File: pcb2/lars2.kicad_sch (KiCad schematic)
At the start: 35 parts, among them SW1 Encoder, SW10 SW_Push, SW2 SW_Push, SW3 SW_Push, SW4 SW_Push, SW5 SW_Push, SW6 SW_Push, SW7 SW_Push, SW8 SW_Push, SW9 SW_Push, U1 Pico, U2 Charger, U3 MOSFET, U4 MOSFET, U5 MOSFET, U6 STEP_UP, U7 STEP_UP, U8 STEP_UP

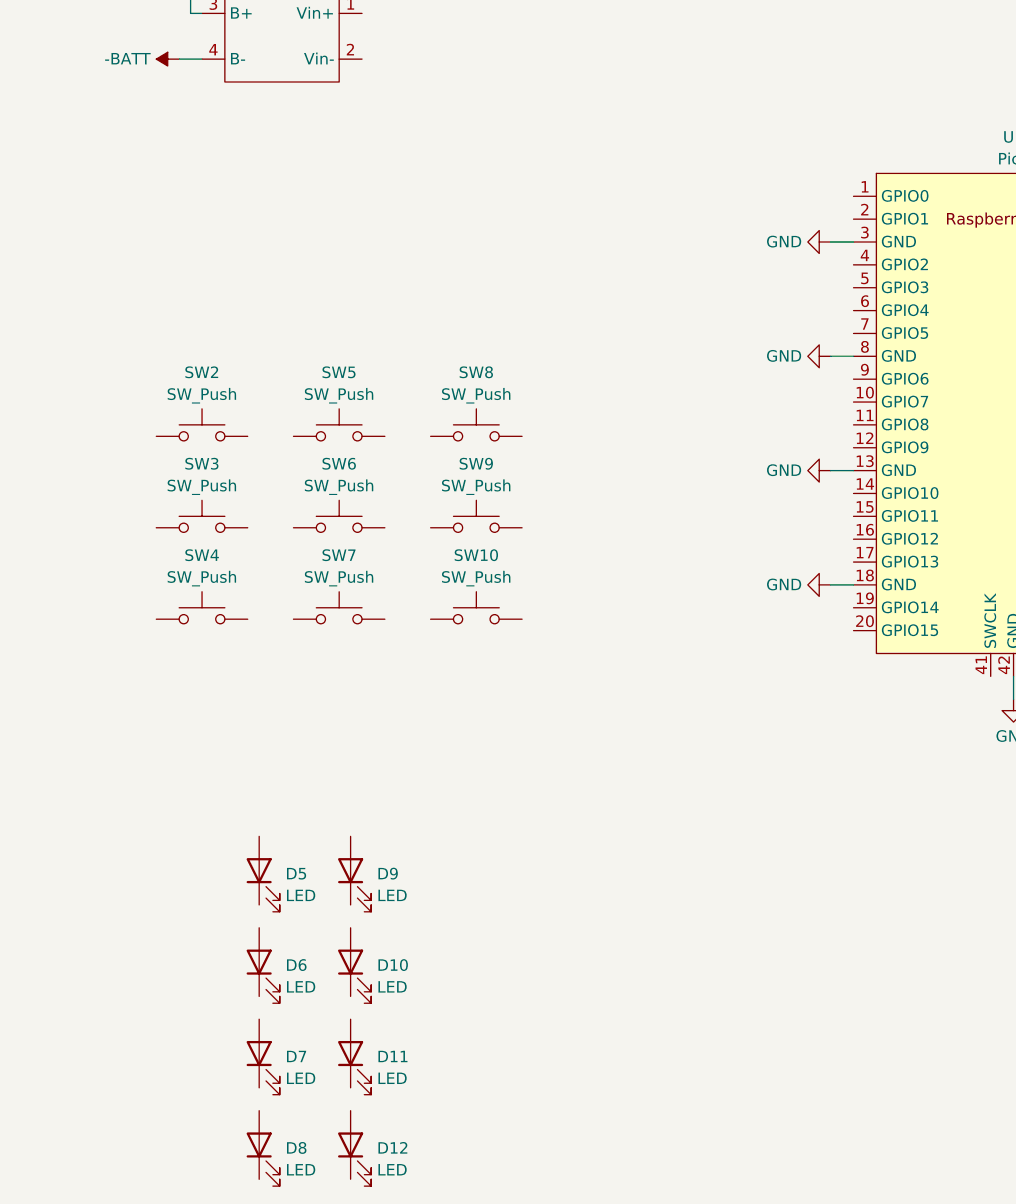
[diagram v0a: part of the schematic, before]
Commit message: finish pcb2, now with buttons and leds
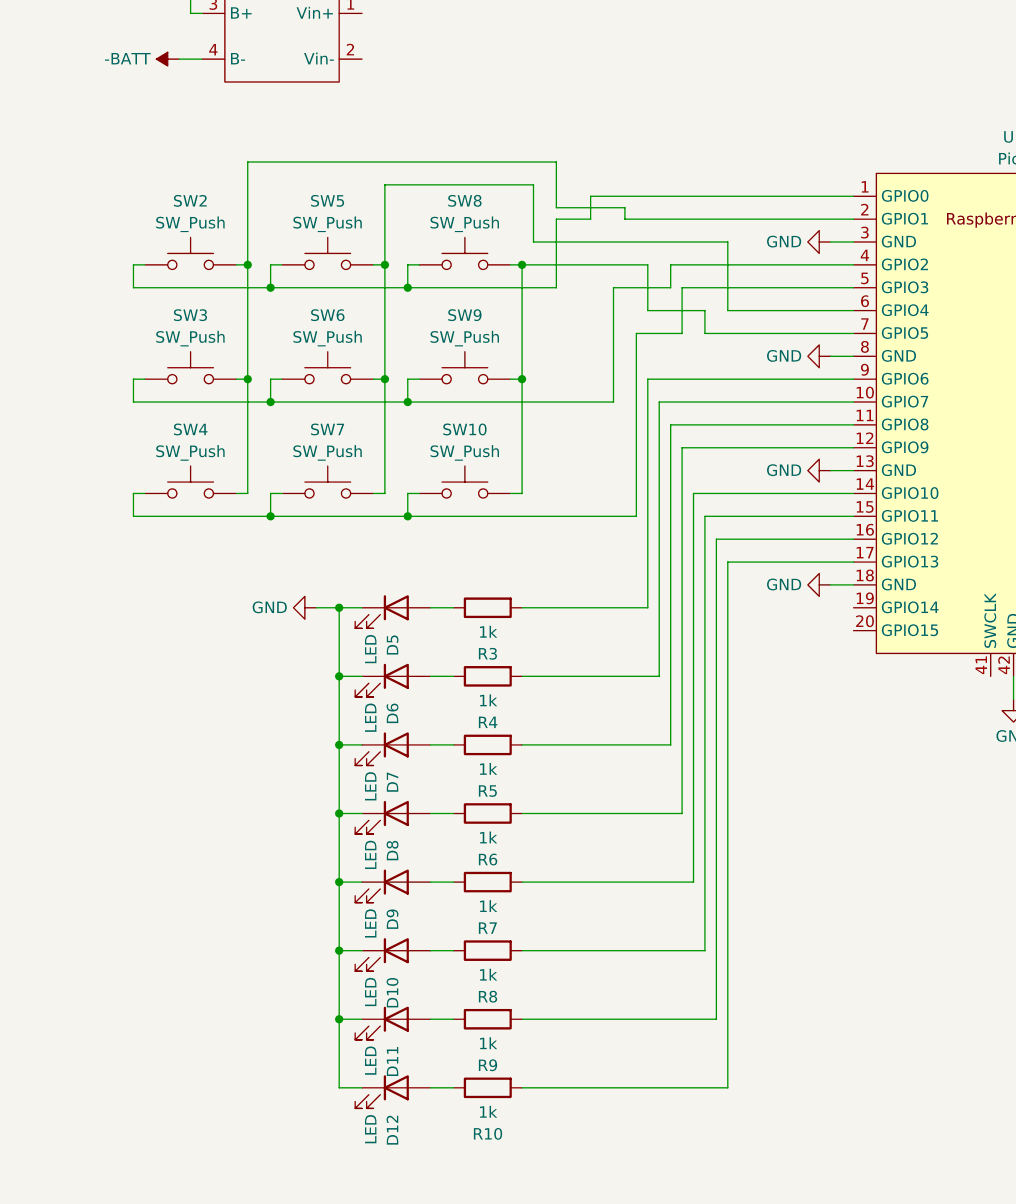
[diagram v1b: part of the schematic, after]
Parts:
- added R10, R3, R4, R5, R6, R7, R8, R9: 1k, Resistor_THT:R_Axial_DIN0204_L3.6mm_D1.6mm_P2.54mm_Vertical, symbol Device:R
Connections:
- net -BATT: now also D10.1 (K), D11.1 (K), D12.1 (K), D5.1 (K), D6.1 (K), D7.1 (K), D8.1 (K), D9.1 (K)
- net at D11.2 (A): now also R9.1
- net at D6.2 (A): now also R4.1
- net at SW3.1: now also SW6.1, SW9.1, U1.4 (GPIO2)
- net at SW3.2: now also SW2.2, SW4.2, U1.2 (GPIO1)
- net at SW7.1: now also SW10.1, SW4.1, U1.5 (GPIO3)
- net at SW7.2: now also SW5.2, SW6.2, U1.6 (GPIO4)
- net at D9.2 (A): now also R7.1
- net at SW2.1: now also SW5.1, SW8.1, U1.1 (GPIO0)
- net at D10.2 (A): now also R8.1
- net at SW10.2: now also SW8.2, SW9.2, U1.7 (GPIO5)
- net at D5.2 (A): now also R3.1
- net at D8.2 (A): now also R6.1
- net at D12.2 (A): now also R10.1
- net at D7.2 (A): now also R5.1
- net at U1.10 (GPIO7): now also R4.2
- net at U1.11 (GPIO8): now also R5.2
- net at U1.12 (GPIO9): now also R6.2
- net at U1.14 (GPIO10): now also R7.2
- net at U1.15 (GPIO11): now also R8.2
- net at U1.16 (GPIO12): now also R9.2
- net at U1.17 (GPIO13): now also R10.2
- net at U1.9 (GPIO6): now also R3.2
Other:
- moved on the sheet: D10, D11, D12, D5, D6, D7, D8, D9, SW10, SW2, SW3, SW4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

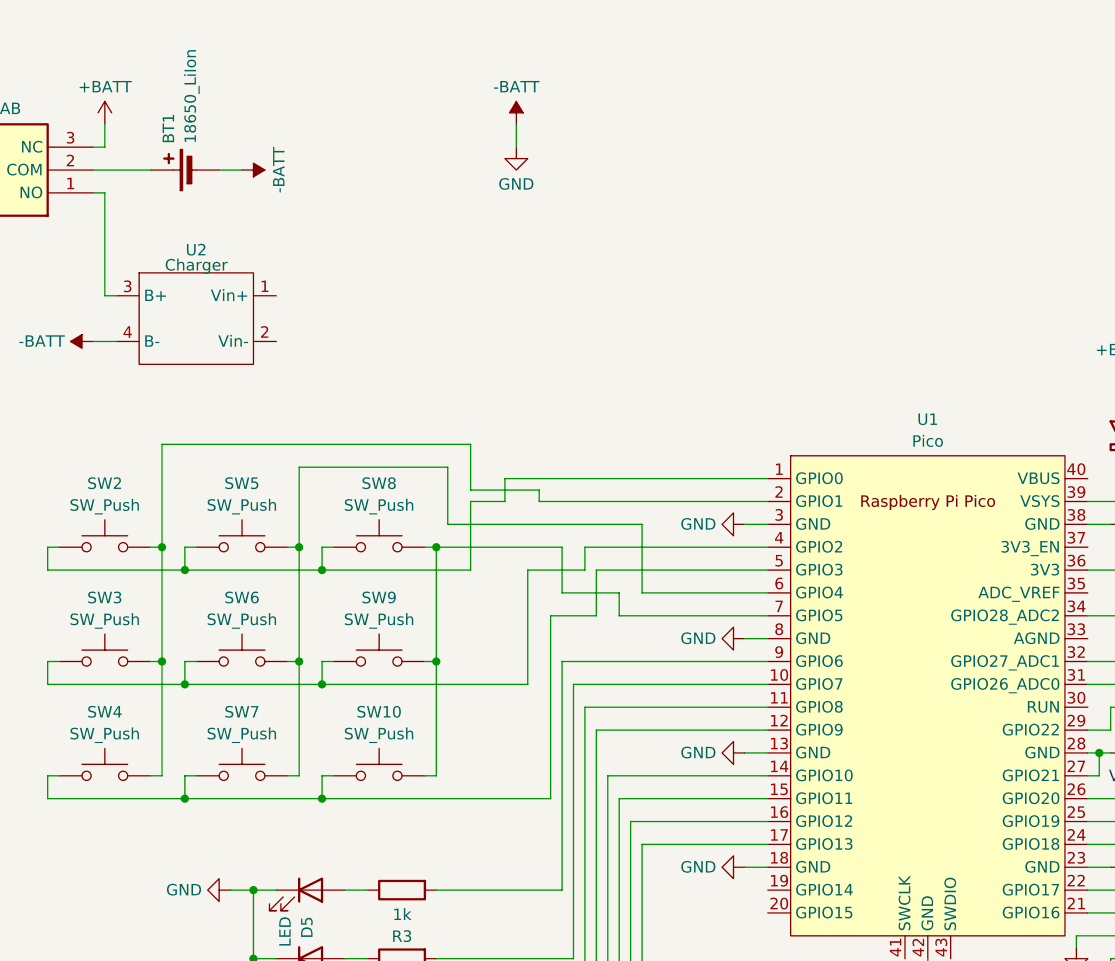
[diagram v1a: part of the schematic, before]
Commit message: lars2 revision 2: use tht footprint for pi pico. improve optics of schematics matrix wiring.
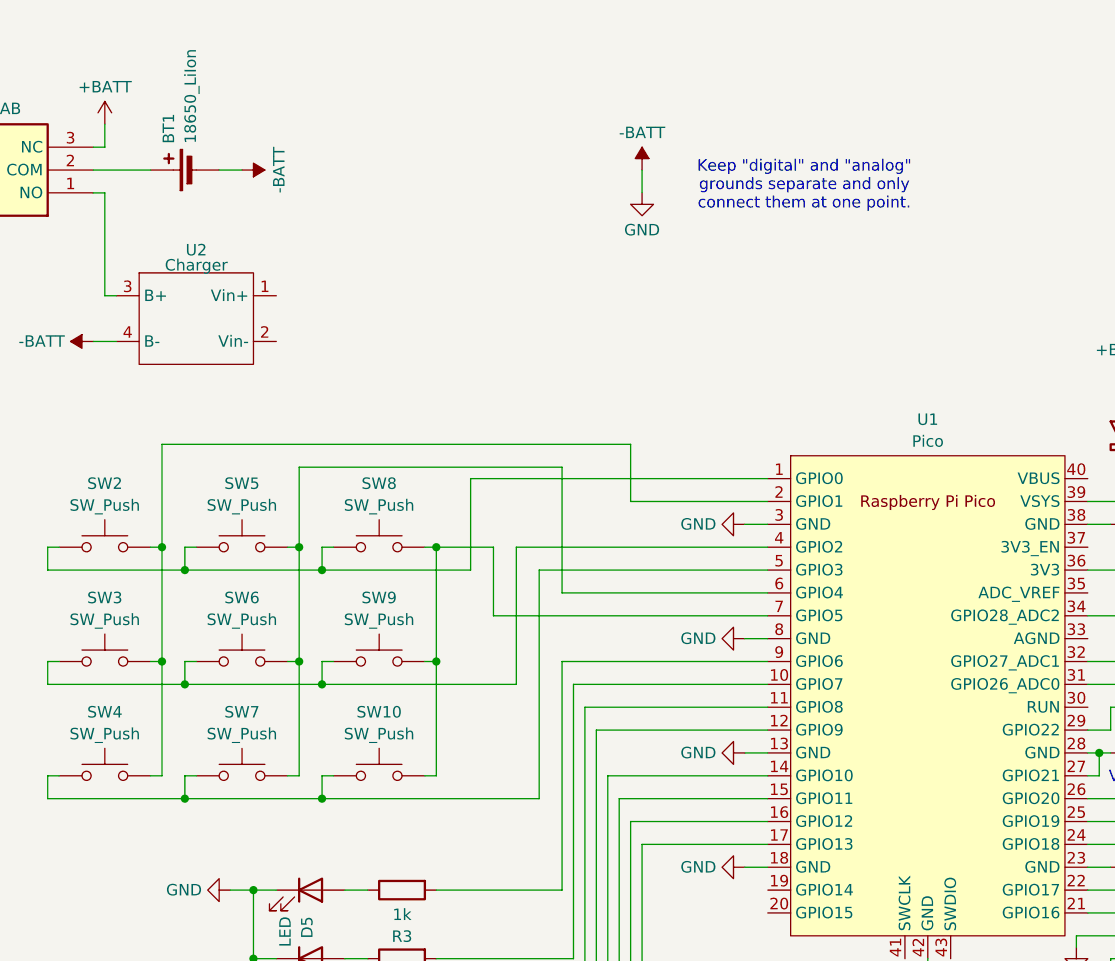
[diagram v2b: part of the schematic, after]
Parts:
- U1: footprint KiCad-RP-Pico:RPi_Pico_SMD_only -> KiCad-RP-Pico:RPi_Pico_SMD_TH
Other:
- note added: "Keep "digital" and "analog" grounds separate and only connect them at one point."
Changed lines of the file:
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@@
 	(title_block
 		(title "LARS V2")
-		(date "2024-04-01")
-		(rev "1")
+		(date "2024-05-14")
+		(rev "2")
 		(comment 1 "https://git.xythobuz.de/thomas/drumkit")
 		(comment 2 "Licensed under the CERN-OHL-S-2.0+")
@@
 	(wire
 		(pts
-			(xy 97.79 76.2) (xy 118.11 76.2)
-		)
-		(stroke
-			(width 0)
-			(type default)
-		)
-	)
-	(wire
-		(pts
 			(xy 233.68 62.23) (xy 233.68 63.5)
 		)
@@
 	(wire
 		(pts
-			(xy 95.25 81.28) (xy 101.6 81.28)
+			(xy 87.63 83.82) (xy 118.11 83.82)
 		)
 		(stroke
@@
 	(wire
 		(pts
-			(xy 93.98 83.82) (xy 93.98 104.14)
+			(xy 92.71 78.74) (xy 92.71 104.14)
 		)
 		(stroke
@@
 	(wire
 		(pts
-			(xy 95.25 81.28) (xy 95.25 76.2)
+			(xy 87.63 83.82) (xy 87.63 76.2)
 		)
 		(stroke
@@
 	(wire
 		(pts
-			(xy 92.71 71.12) (xy 118.11 71.12)
+			(xy 102.87 71.12) (xy 118.11 71.12)
 		)
 		(stroke
@@
 	(wire
 		(pts
-			(xy 104.14 81.28) (xy 104.14 73.66)
+			(xy 95.25 81.28) (xy 95.25 67.31)
 		)
 		(stroke
@@
 	(wire
 		(pts
-			(xy 90.17 29.21) (xy 90.17 31.75)
+			(xy 104.14 34.29) (xy 104.14 36.83)
 		)
 		(stroke
@@
 	(wire
 		(pts
-			(xy 85.09 69.85) (xy 92.71 69.85)
-		)
-		(stroke
-			(width 0)
-			(type default)
-		)
-	)
-	(wire
-		(pts
 			(xy 185.42 115.57) (xy 185.42 119.38)
 		)
@@
 	(wire
 		(pts
-			(xy 95.25 76.2) (xy 81.28 76.2)
+			(xy 87.63 76.2) (xy 81.28 76.2)
 		)
 		(stroke
@@
 	(wire
 		(pts
-			(xy 88.9 71.12) (xy 88.9 68.58)
+			(xy 85.09 68.58) (xy 85.09 78.74)
 		)
 		(stroke
@@
 	(wire
 		(pts
-			(xy 82.55 67.31) (xy 66.04 67.31)
+			(xy 66.04 67.31) (xy 95.25 67.31)
 		)
 		(stroke
@@
 	(wire
 		(pts
-			(xy 101.6 83.82) (xy 118.11 83.82)
-		)
-		(stroke
-			(width 0)
-			(type default)
-		)
-	)
-	(wire
-		(pts
 			(xy 99.06 96.52) (xy 99.06 137.16)
 		)
@@
 	(wire
 		(pts
-			(xy 82.55 73.66) (xy 104.14 73.66)
-		)
-		(stroke
-			(width 0)
-			(type default)
-		)
-	)
-	(wire
-		(pts
 			(xy 60.96 121.92) (xy 63.5 121.92)
 		)
@@
 	(wire
 		(pts
-			(xy 118.11 78.74) (xy 99.06 78.74)
-		)
-		(stroke
-			(width 0)
-			(type default)
-		)
-	)
-	(wire
-		(pts
 			(xy 153.67 111.76) (xy 156.21 111.76)
 		)
@@
 	(wire
 		(pts
-			(xy 85.09 71.12) (xy 85.09 78.74)
-		)
-		(stroke
-			(width 0)
-			(type default)
-		)
-	)
-	(wire
-		(pts
 			(xy 177.8 109.22) (xy 176.53 109.22)
 		)
@@
 	(wire
 		(pts
-			(xy 68.58 91.44) (xy 91.44 91.44)
+			(xy 68.58 91.44) (xy 90.17 91.44)
 		)
 		(stroke
@@
 	(wire
 		(pts
-			(xy 92.71 69.85) (xy 92.71 71.12)
+			(xy 102.87 64.77) (xy 102.87 71.12)
 		)
 		(stroke
@@
 	(wire
 		(pts
-			(xy 85.09 71.12) (xy 88.9 71.12)
-		)
-		(stroke
-			(width 0)
-			(type default)
-		)
-	)
-	(wire
-		(pts
 			(xy 71.12 129.54) (xy 73.66 129.54)
 		)
@@
 	(wire
 		(pts
-			(xy 99.06 83.82) (xy 93.98 83.82)
+			(xy 92.71 78.74) (xy 118.11 78.74)
 		)
 		(stroke
@@
 	(wire
 		(pts
-			(xy 91.44 78.74) (xy 97.79 78.74)
+			(xy 90.17 76.2) (xy 118.11 76.2)
 		)
 		(stroke
@@
 	(wire
 		(pts
-			(xy 88.9 68.58) (xy 118.11 68.58)
+			(xy 85.09 68.58) (xy 118.11 68.58)
 		)
 		(stroke
@@
 	(wire
 		(pts
-			(xy 85.09 64.77) (xy 50.8 64.77)
+			(xy 102.87 64.77) (xy 50.8 64.77)
 		)
 		(stroke
@@
 	(wire
 		(pts
-			(xy 101.6 81.28) (xy 101.6 83.82)
-		)
-		(stroke
-			(width 0)
-			(type default)
-		)
-	)
-	(wire
-		(pts
 			(xy 50.8 88.9) (xy 50.8 101.6)
 		)
@@
 	(wire
 		(pts
-			(xy 68.58 104.14) (xy 93.98 104.14)
+			(xy 68.58 104.14) (xy 92.71 104.14)
 		)
 		(stroke
@@
 	(wire
 		(pts
-			(xy 97.79 78.74) (xy 97.79 76.2)
-		)
-		(stroke
-			(width 0)
-			(type default)
-		)
-	)
-	(wire
-		(pts
 			(xy 233.68 107.95) (xy 233.68 109.22)
 		)
@@
 	(wire
 		(pts
-			(xy 82.55 73.66) (xy 82.55 67.31)
-		)
-		(stroke
-			(width 0)
-			(type default)
-		)
-	)
-	(wire
-		(pts
 			(xy 252.73 101.6) (xy 255.27 101.6)
 		)
@@
 	(wire
 		(pts
-			(xy 85.09 64.77) (xy 85.09 69.85)
-		)
-		(stroke
-			(width 0)
-			(type default)
-		)
-	)
-	(wire
-		(pts
 			(xy 49.53 88.9) (xy 50.8 88.9)
 		)
@@
 	(wire
 		(pts
-			(xy 118.11 81.28) (xy 104.14 81.28)
+			(xy 118.11 81.28) (xy 95.25 81.28)
 		)
 		(stroke
@@
 	(wire
 		(pts
-			(xy 99.06 78.74) (xy 99.06 83.82)
-		)
-		(stroke
-			(width 0)
-			(type default)
-		)
-	)
-	(wire
-		(pts
 			(xy 156.21 96.52) (xy 153.67 96.52)
 		)
@@
 	(wire
 		(pts
-			(xy 91.44 78.74) (xy 91.44 91.44)
+			(xy 90.17 76.2) (xy 90.17 91.44)
 		)
 		(stroke
@@
 		)
 	)
+	(text "Keep \"digital\" and \"analog\"\ngrounds separate and only\nconnect them at one point."
+		(exclude_from_sim no)
+		(at 122.174 36.068 0)
+		(effects
+			(font
+				(size 1.27 1.27)
+			)
+		)
+	)
 	(text "V2 HW Indicator"
 		(exclude_from_sim no)
@@
 	(symbol
 		(lib_id "power:-BATT")
-		(at 90.17 29.21 0)
+		(at 104.14 34.29 0)
 		(unit 1)
 		(exclude_from_sim no)
@@
 		(fields_autoplaced yes)
 		(property "Reference" "#PWR020"
-			(at 90.17 33.02 0)
+			(at 104.14 38.1 0)
 			(effects
 				(font
@@
 		)
 		(property "Value" "-BATT"
-			(at 90.17 25.0769 0)
+			(at 104.14 30.1569 0)
 			(effects
 				(font
@@
 		)
 		(property "Footprint" ""
-			(at 90.17 29.21 0)
+			(at 104.14 34.29 0)
 			(effects
 				(font
@@
 		)
 		(property "Datasheet" ""
-			(at 90.17 29.21 0)
+			(at 104.14 34.29 0)
 			(effects
 				(font
@@
 		)
 		(property "Description" "Power symbol creates a global label with name \"-BATT\""
-			(at 90.17 29.21 0)
+			(at 104.14 34.29 0)
 			(effects
 				(font
@@
 	(symbol
 		(lib_id "power:GND")
-		(at 90.17 31.75 0)
+		(at 104.14 36.83 0)
 		(unit 1)
 		(exclude_from_sim no)
@@
 		(fields_autoplaced yes)
 		(property "Reference" "#PWR019"
-			(at 90.17 38.1 0)
+			(at 104.14 43.18 0)
 			(effects
 				(font
@@
 		)
 		(property "Value" "GND"
-			(at 90.17 35.8831 0)
+			(at 104.14 40.9631 0)
 			(effects
 				(font
@@
 		)
 		(property "Footprint" ""
-			(at 90.17 31.75 0)
+			(at 104.14 36.83 0)
 			(effects
 				(font
@@
 		)
 		(property "Datasheet" ""
-			(at 90.17 31.75 0)
+			(at 104.14 36.83 0)
 			(effects
 				(font
@@
 		)
 		(property "Description" "Power symbol creates a global label with name \"GND\" , ground"
-			(at 90.17 31.75 0)
+			(at 104.14 36.83 0)
 			(effects
 				(font
@@
 			)
 		)
-		(property "Footprint" "KiCad-RP-Pico:RPi_Pico_SMD_only"
+		(property "Footprint" "KiCad-RP-Pico:RPi_Pico_SMD_TH"
 			(at 135.89 92.71 90)
 			(effects
